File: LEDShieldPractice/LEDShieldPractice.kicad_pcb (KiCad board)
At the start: 2 copper layers, 40.3 x 64.1 mm, 24 parts, among them J1 Conn_02x05_Odd_Even, J2 CLOCK_IN, Q1 2N3904

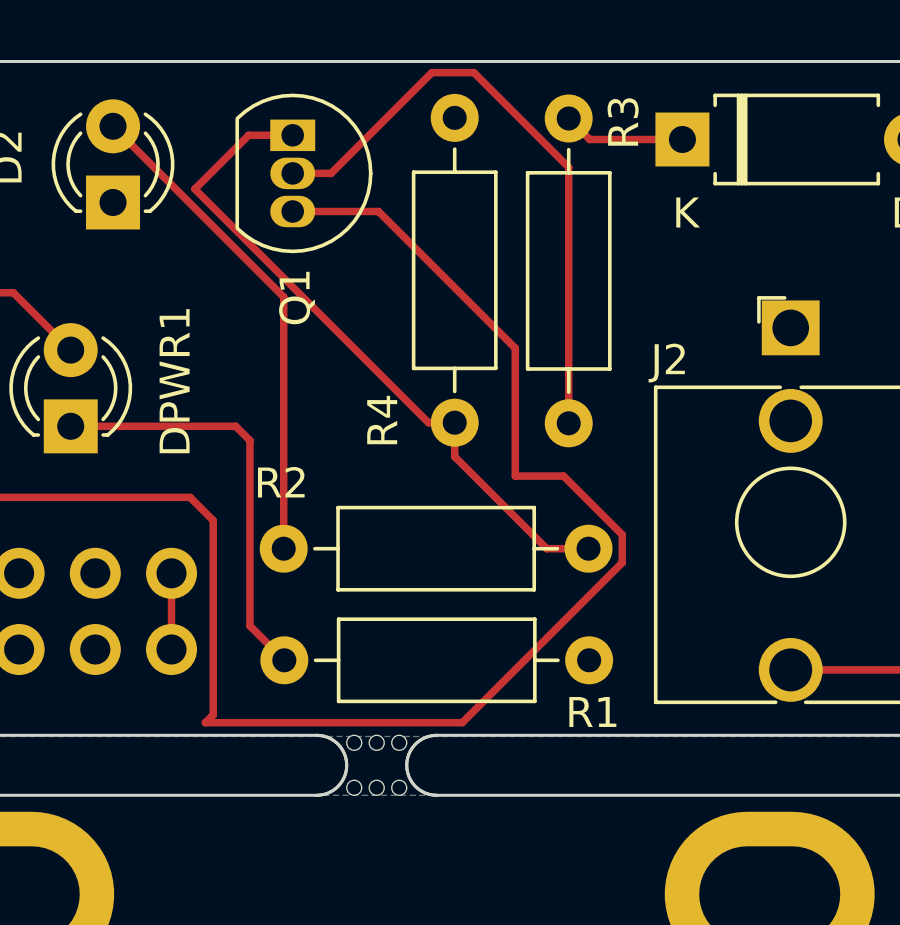
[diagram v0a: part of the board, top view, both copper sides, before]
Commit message: Start moving components to surface mount
Looking at Super16 project I think maybe I mounted my transistor incorrectly and that I should probably voltage divide the input to it significantly.  OR I used a PNP instead of NPN transistor, need to doublecheck. The current build dims the led on a clock signal instead of illuminating.
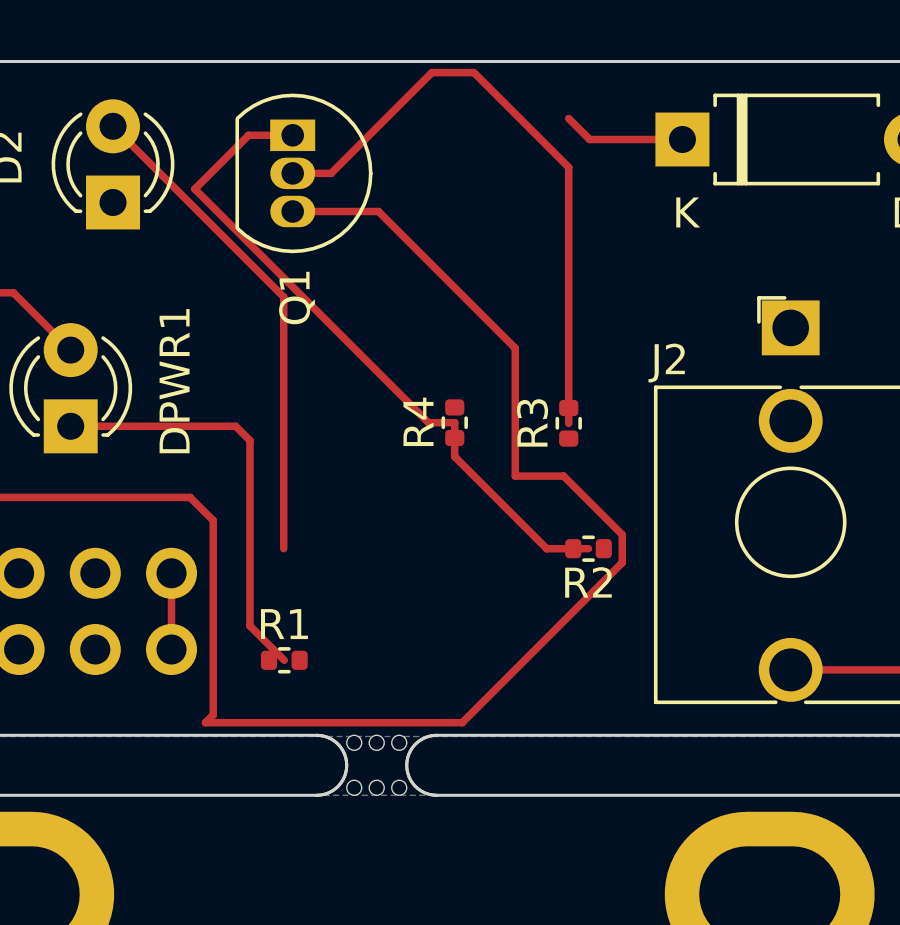
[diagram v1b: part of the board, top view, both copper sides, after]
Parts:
- R1, R2, R3, R4: footprint Resistor_THT:R_Axial_DIN0207_L6.3mm_D2.5mm_P10.16mm_Horizontal -> Resistor_SMD:R_0402_1005Metric
